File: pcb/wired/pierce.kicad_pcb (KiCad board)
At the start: 2 copper layers, 115 x 91.4 mm, 36 parts, among them SW11 SW_PUSH, SW12 SW_PUSH, SW13 SW_PUSH, SW14 SW_PUSH, SW19 SW_PUSH, SW20 SW_PUSH, SW21 SW_PUSH, SW22 SW_PUSH, SW27 SW_PUSH, SW28 SW_PUSH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

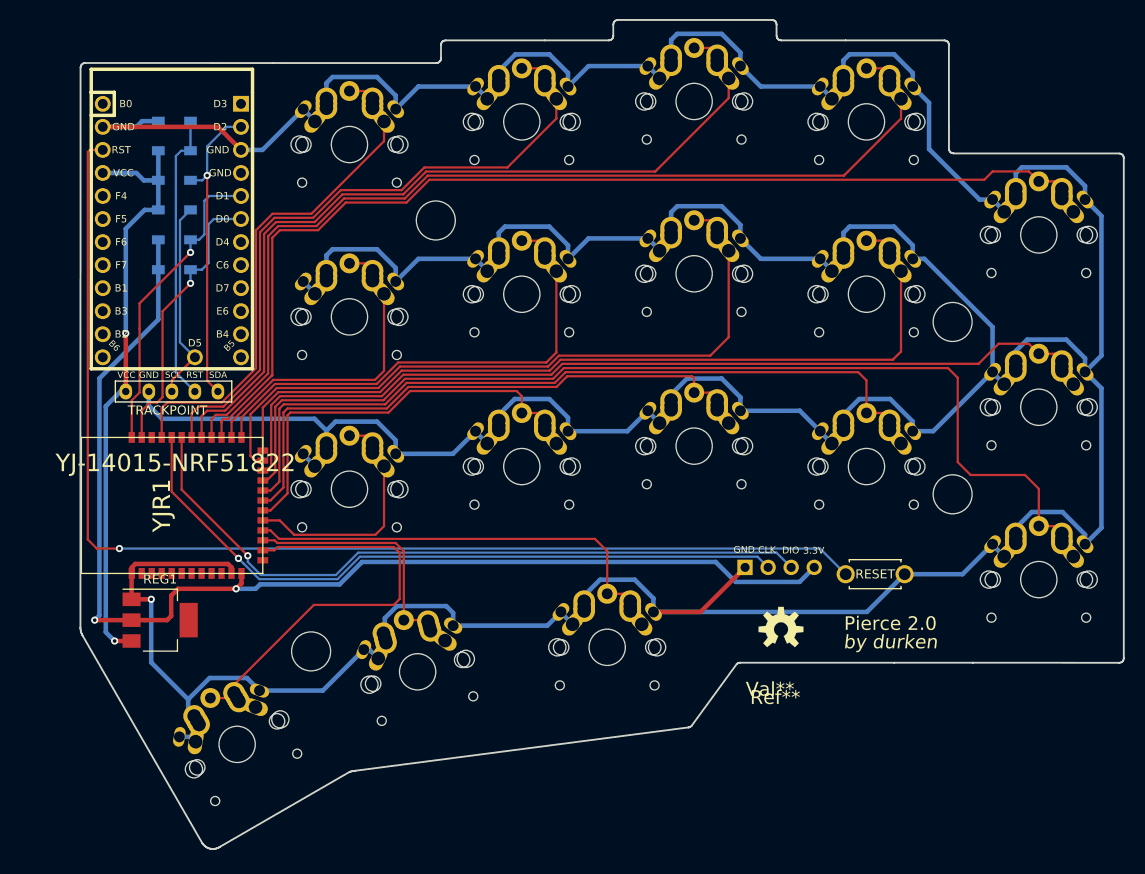
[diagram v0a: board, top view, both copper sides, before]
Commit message: add reciever pcb for dual wireless setup
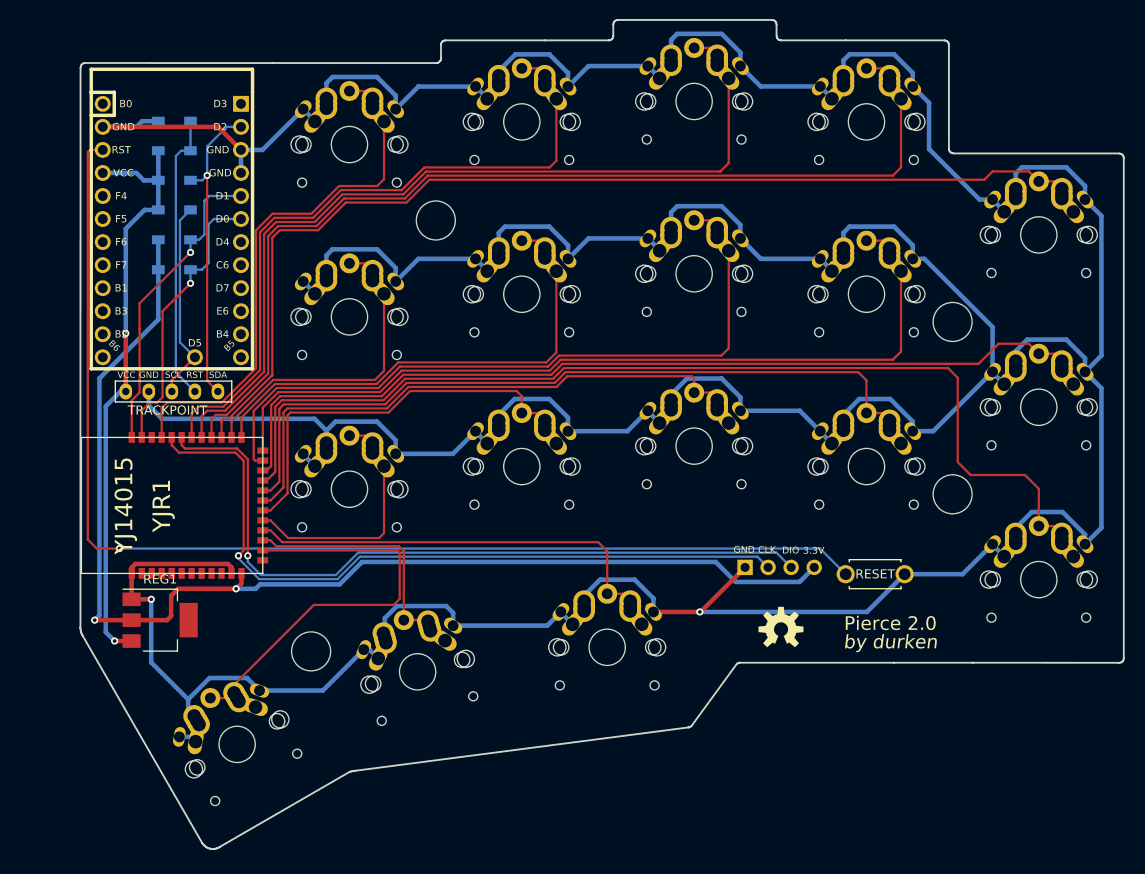
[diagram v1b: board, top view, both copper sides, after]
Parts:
- YJR1: value YJ-14015-NRF51822 -> YJ14015
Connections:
- net GND_R renamed GND
- net VCC_R_3.3V renamed VCC_3.3V
- net VCC_R_5V renamed VCC_5V
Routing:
- net SW02R: track 90.9 -> 95.1 mm
- net CLKR: track 77.2 -> 81.4 mm
- net DIOR: track 78.9 -> 82.3 mm
- net SW03R: track 108.2 -> 111.3 mm
- net SW01R: track 72.3 -> 75.0 mm
- net SW00R: track 55.9 -> 58.3 mm
- net SW20R: track 25.9 -> 26.6 mm
- net GND: track 622.6 -> 621.9 mm, vias 1 -> 2

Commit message: small adjustments
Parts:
- moved R4 2.34 mm to (157.5, 53.8)
- moved R5 2.34 mm to (157.5, 50.5)
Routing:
- net VCC_5V: track 66.4 -> 69.2 mm, vias 2 -> 1
- net VCC_3.3V: track 131.6 -> 129.3 mm
- net I2C_SDA: track 34.2 -> 33.0 mm
- net I2C_SCL: track 31.6 -> 30.6 mm
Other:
- board text added: "trackpoint"

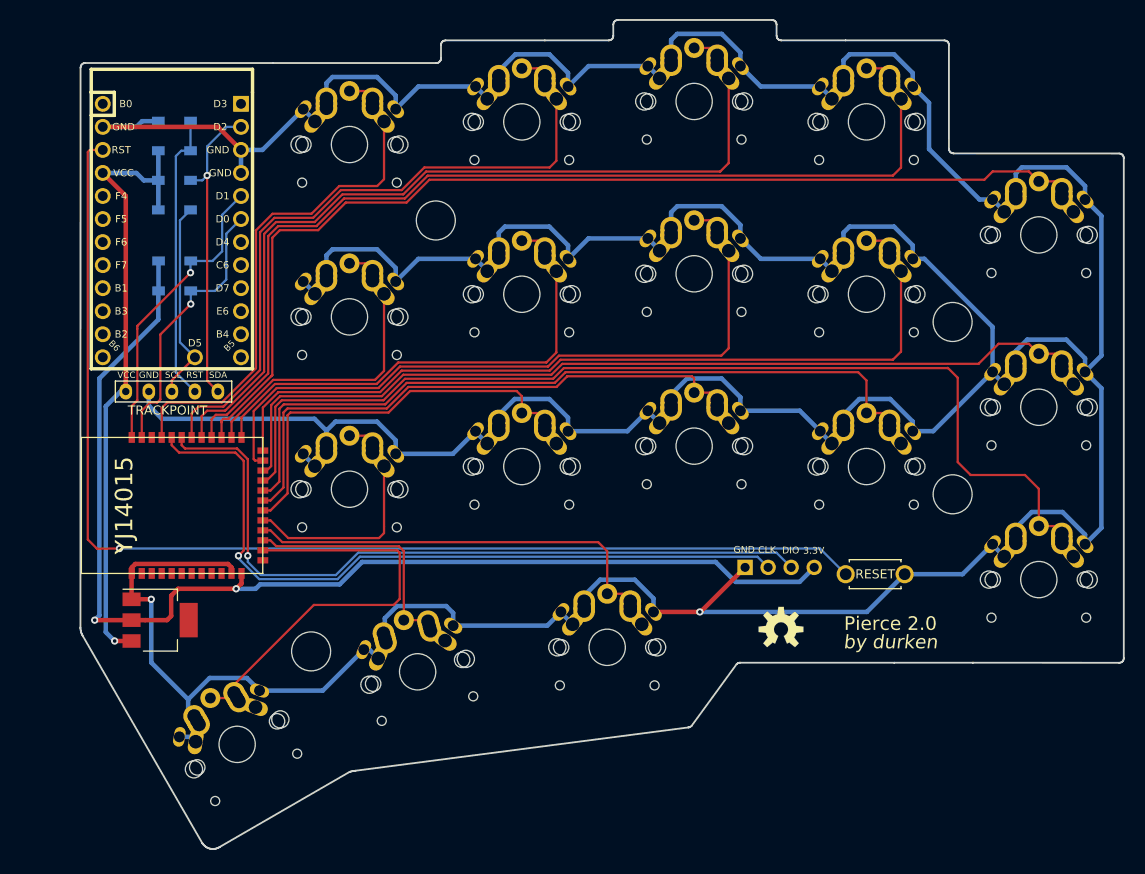
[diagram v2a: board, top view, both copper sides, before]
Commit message: add gnd planes
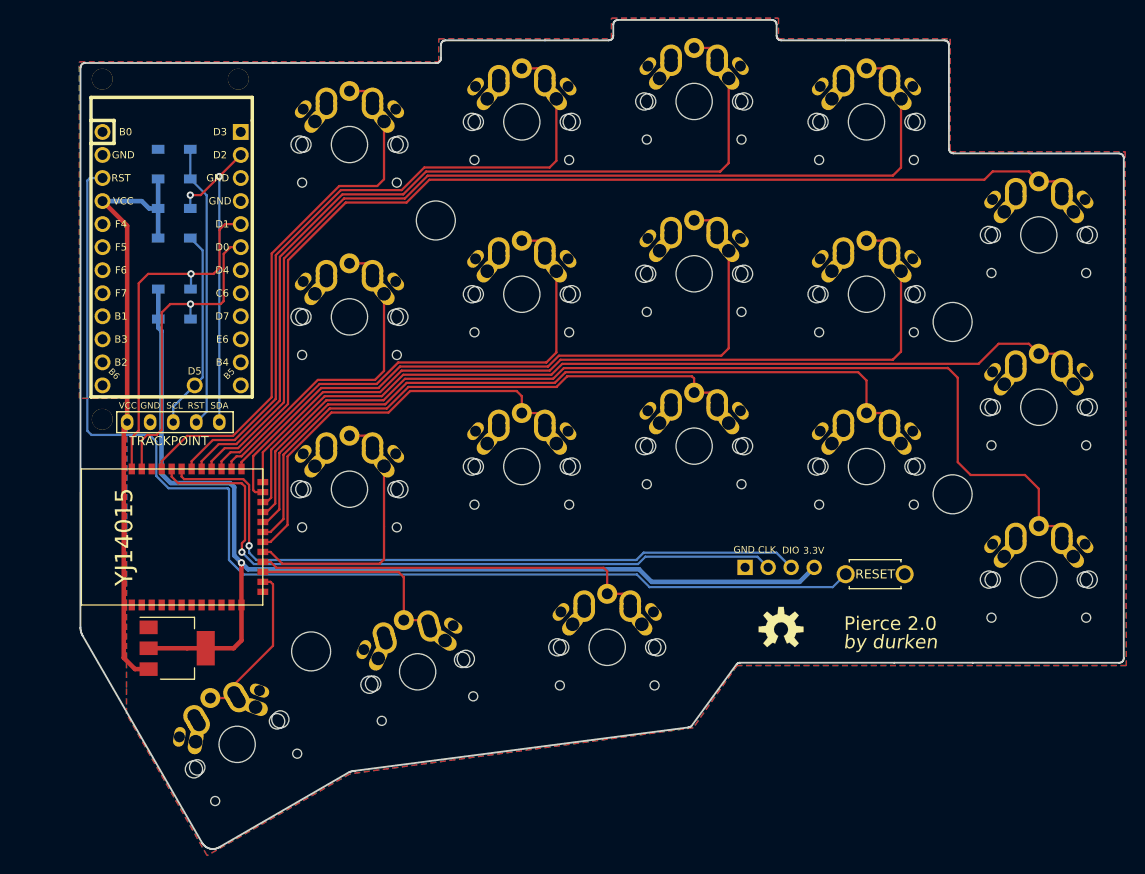
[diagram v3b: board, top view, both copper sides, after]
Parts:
- added Ref**: Val**, kbd:M2_Threads_v2, F.Cu at (164.5, 30.5)
- added Ref**: Val**, kbd:M2_Threads_v2, F.Cu at (149.5, 30.5)
- added Ref**: Val**, kbd:M2_Threads_v2, F.Cu at (149.5, 68.0)
- moved REG1 3.62 mm to (157.8, 93.2)
- moved YJR1 3.48 mm to (167.2, 81.0)
- moved TP1 3.38 mm to (152.2, 68.3)
- moved R1 3.10 mm to (157.4, 38.2)
- moved R2 3.10 mm to (157.4, 48.0)
- moved AVR1 3.10 mm to (156.9, 50.3)
- moved R4 3.10 mm to (157.5, 56.9)
- moved C1 3.10 mm to (157.4, 41.5)
- moved R3 3.10 mm to (157.4, 44.8)
- moved R5 3.10 mm to (157.5, 53.6)
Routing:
- net GND: track 621.9 -> 0.03 mm, vias 2 -> 0
- net SW30R: track 50.4 -> 19.9 mm
- net VCC_3.3V: track 129.3 -> 121.7 mm, vias 2 -> 1
- net I2C_SDA: track 33.0 -> 38.9 mm
- net CLKR: track 81.4 -> 76.1 mm
- net DIOR: track 82.3 -> 77.2 mm
- net I2C_SCL: track 30.6 -> 35.2 mm
- net SW31R: track 28.8 -> 25.7 mm
- net SW32R: track 48.5 -> 45.8 mm
- net SW20R: track 26.6 -> 29.2 mm
- net reset: track 129.6 -> 127.5 mm, vias 1 -> 0
- net SDA: track 34.2 -> 36.0 mm, vias 1 -> 2
- net VCC_5V: track 69.2 -> 67.9 mm, vias 1 -> 0
- net SW03R: track 111.3 -> 112.5 mm
- net SW04R: track 117.7 -> 118.8 mm
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- added copper zone on B.Cu, net GND
- added copper zone on F.Cu, net GND

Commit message: small visual adjustments
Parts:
- Ref** (x2): footprint pierce:OSHW-LOGO-M -> pierce:OSHW-Logo2_7.3x6mm_SilkScreen
- moved Ref** 3.68 mm to (227.8, 90.0)
- moved Ref** 3.64 mm to (227.8, 90.0)
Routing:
- net GND: vias 0 -> 1

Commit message: small adjustments
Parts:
- removed the Ref** at (227.8, 90.0) (x2)
- moved RST1 0.75 mm to (234.7, 84.3)
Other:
- outline, holes or cut-outs redrawn
